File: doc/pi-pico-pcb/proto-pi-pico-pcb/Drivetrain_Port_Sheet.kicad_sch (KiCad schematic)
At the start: 1 part

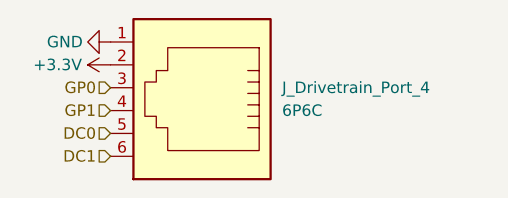
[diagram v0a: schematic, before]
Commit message: added flash memory
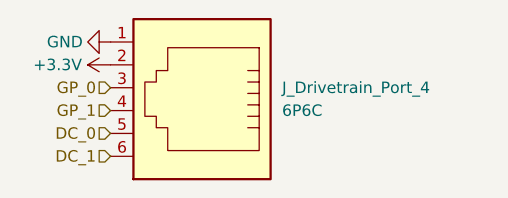
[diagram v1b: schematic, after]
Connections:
- net DC0 renamed DC_0
- net DC1 renamed DC_1
- net GP0 renamed GP_0
- net GP1 renamed GP_1
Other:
- company: (none) -> PROTO
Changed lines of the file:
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@@
 (kicad_sch (version 20211123) (generator eeschema)
   (paper "A4")
-  (hierarchical_label "GP0" (shape input) (at 136.525 96.52 180)
+  (title_block
+    (date "2025-09-09")
+    (rev "1")
+    (company "PROTO")
+    (comment 1 "Author: Carston Wiebe")
+  )
+  (hierarchical_label "GP_0" (shape input) (at 136.525 96.52 180)
     (effects (font (size 1.27 1.27)) (justify right))
   )
-  (hierarchical_label "DC1" (shape input) (at 136.525 104.14 180)
+  (hierarchical_label "DC_1" (shape input) (at 136.525 104.14 180)
     (effects (font (size 1.27 1.27)) (justify right))
   )
-  (hierarchical_label "GP1" (shape input) (at 136.525 99.06 180)
+  (hierarchical_label "GP_1" (shape input) (at 136.525 99.06 180)
     (effects (font (size 1.27 1.27)) (justify right))
   )
-  (hierarchical_label "DC0" (shape input) (at 136.525 101.6 180)
+  (hierarchical_label "DC_0" (shape input) (at 136.525 101.6 180)
     (effects (font (size 1.27 1.27)) (justify right))
   )
